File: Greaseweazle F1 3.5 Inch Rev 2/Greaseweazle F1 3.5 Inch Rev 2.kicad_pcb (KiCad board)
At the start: 2 copper layers, 170.2 x 100 mm, 67 parts, among them CN1 Floppy Data, J1 USB B, J10 Conn_01x03, J11 Conn_01x03, J12 Display Port, J13 Display Port, J2 USB Header, J3 Floppy Power, J4 Floppy Power Header, J5 Programming Port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

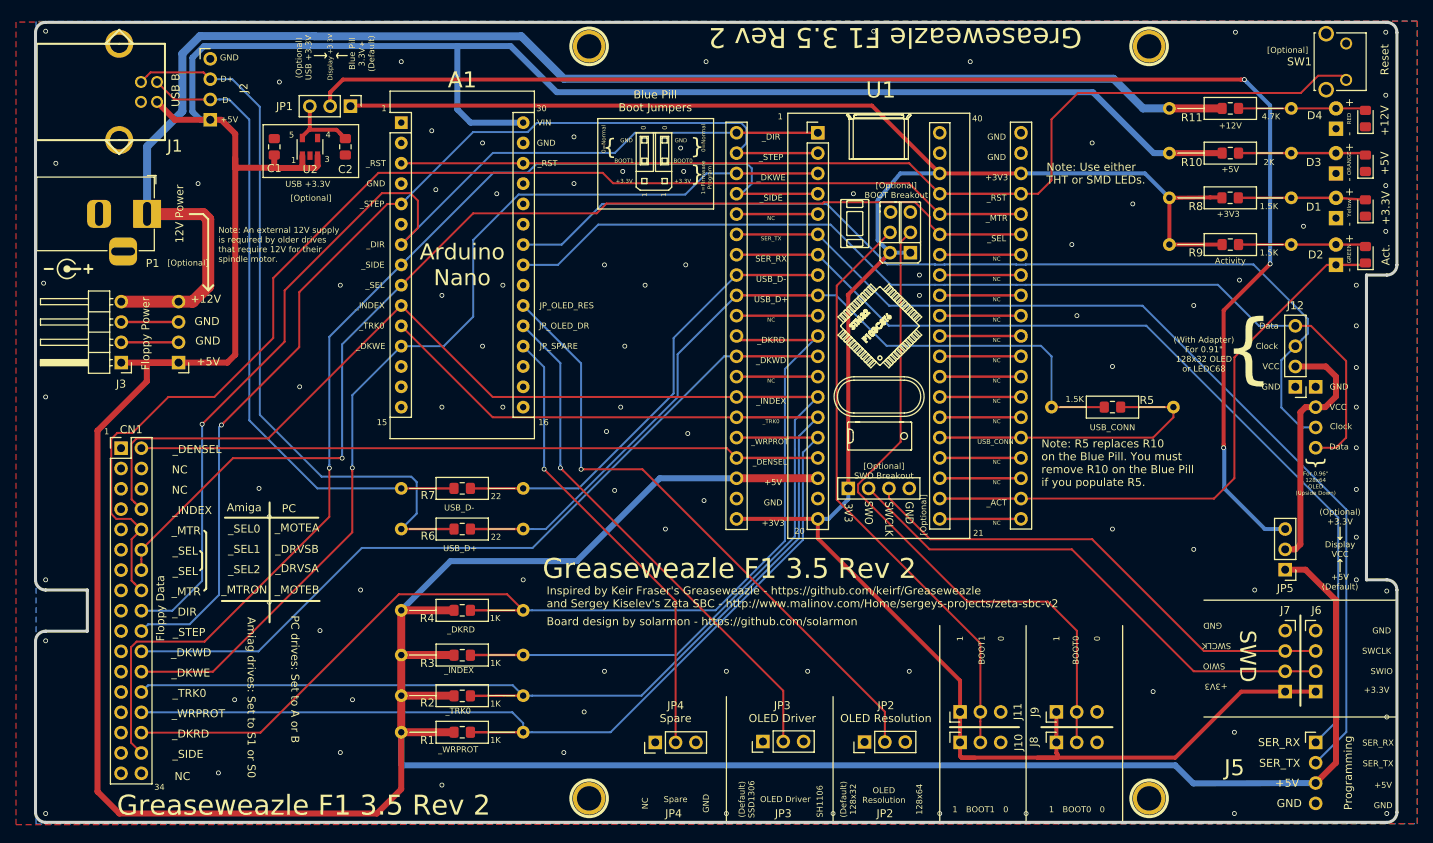
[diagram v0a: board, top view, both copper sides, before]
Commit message: Grounded USB shiled, and improved Arduino Nano silkscreen
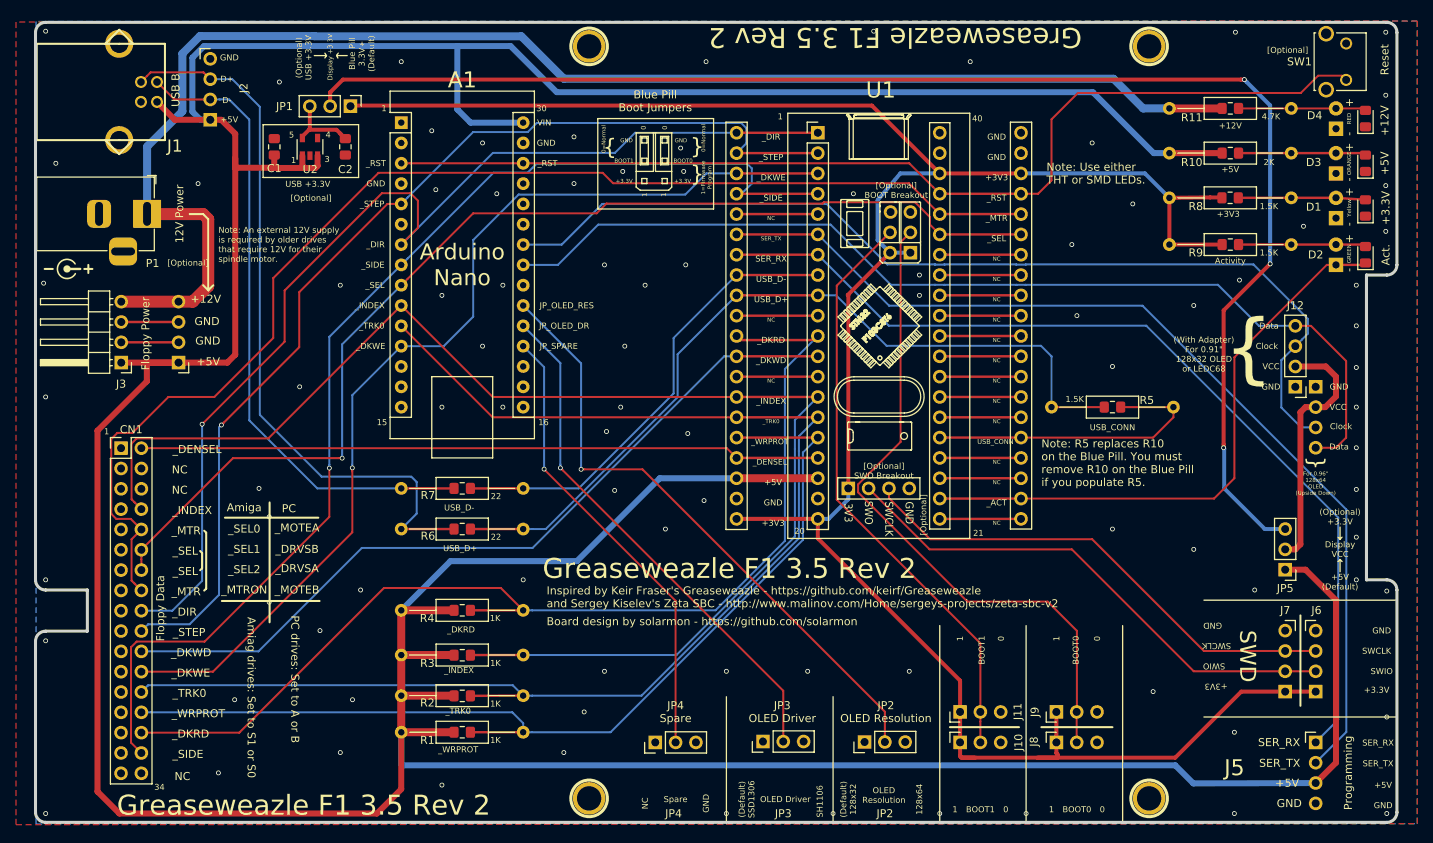
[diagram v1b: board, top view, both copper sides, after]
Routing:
- net /_DKRD: track 137.3 -> 137.9 mm

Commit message: Moved J13 for 0.96 inch OLED further forward
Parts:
- moved Floppy Drive 3.30 mm to (159.0, 100.8)
- moved J13 2.54 mm to (213.4, 96.5)
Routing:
- net /Display_VCC: track 32.3 -> 37.3 mm
- net /Display_Clock: track 123.9 -> 126.5 mm
- net /Display_Data: track 125.9 -> 126.8 mm
- net GND: vias 94 -> 93
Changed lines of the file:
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@@
     (thickness 1.6)
     (drawings 348)
-    (tracks 645)
+    (tracks 643)
     (zones 0)
     (modules 67)
@@
   )
   (module Connector_PinHeader_2.54mm:PinHeader_1x04_P2.54mm_Vertical (layer B.Cu)
-    (at 210.82 96.52 180)
+    (at 213.36 96.52 180)
     (descr "Through hole straight pin header, 1x04, 2.54mm pitch, single row")
     (tags "Through hole pin header THT 1x04 2.54mm single row")
@@
   )
   (module solarmon_library:Floppy_Drive locked (layer F.Cu)
-    (at 155.702 100.838)
+    (at 159 100.838)
     (fp_text reference "Floppy Drive" (at 0.254 -2.032) (layer Dwgs.User)
       (effects (font (size 1 1) (thickness 0.15)))
@@
   (gr_line (start 213.868 118.11) (end 214.122 118.364) (layer F.SilkS) (width 0.12))
   (gr_line (start 213.868 119.634) (end 213.868 118.11) (layer F.SilkS) (width 0.12))
-  (gr_text { (at 210.693 106.045 90) (layer F.SilkS)
+  (gr_text { (at 213.1314 106.3244 90) (layer F.SilkS)
     (effects (font (size 2 2) (thickness 0.125)))
   )
@@
     (effects (font (size 7 7) (thickness 0.125)))
   )
-  (gr_text "For 0.96\"\n128x64\nOLED\n(Upside Down)" (at 210.82 108.585) (layer F.SilkS)
+  (gr_text "For 0.96\"\n128x64\nOLED\n(Upside Down)" (at 213.2584 108.8644) (layer F.SilkS)
     (effects (font (size 0.5 0.5) (thickness 0.125)))
   )
@@
     (effects (font (size 0.75 0.75) (thickness 0.125)))
   )
-  (gr_text Data (at 213.741 104.013) (layer F.SilkS)
+  (gr_text Data (at 215.773 104.0638) (layer F.SilkS)
     (effects (font (size 0.75 0.75) (thickness 0.125)))
   )
-  (gr_text Clock (at 213.995 101.473) (layer F.SilkS)
-    (effects (font (size 0.75 0.75) (thickness 0.125)))
+  (gr_text Clock (at 215.8238 101.6254) (layer F.SilkS)
+    (effects (font (size 0.6 0.6) (thickness 0.125)))
   )
-  (gr_text VCC (at 213.614 99.06) (layer F.SilkS)
-    (effects (font (size 0.75 0.75) (thickness 0.125)))
+  (gr_text VCC (at 215.8492 99.06) (layer F.SilkS)
+    (effects (font (size 0.6 0.6) (thickness 0.125)))
   )
-  (gr_text GND (at 213.741 96.52) (layer F.SilkS)
-    (effects (font (size 0.75 0.75) (thickness 0.125)))
+  (gr_text GND (at 215.773 96.4946) (layer F.SilkS)
+    (effects (font (size 0.6 0.6) (thickness 0.125)))
   )
   (gr_text Data (at 204.978 88.9) (layer F.SilkS)
@@
   (via (at 215.9 83.82) (size 0.6) (drill 0.4) (layers F.Cu B.Cu) (net 1))
   (via (at 215.9 88.9) (size 0.6) (drill 0.4) (layers F.Cu B.Cu) (net 1))
-  (via (at 215.9 94.107) (size 0.6) (drill 0.4) (layers F.Cu B.Cu) (net 1))
-  (via (at 215.9 99.06) (size 0.6) (drill 0.4) (layers F.Cu B.Cu) (net 1))
-  (via (at 215.9 104.14) (size 0.6) (drill 0.4) (layers F.Cu B.Cu) (net 1))
+  (via (at 215.9 91.44) (size 0.6) (drill 0.4) (layers F.Cu B.Cu) (net 1))
+  (via (at 215.9 106.68) (size 0.6) (drill 0.4) (layers F.Cu B.Cu) (net 1))
   (via (at 215.9 109.347) (size 0.6) (drill 0.4) (layers F.Cu B.Cu) (net 1))
   (via (at 215.9 115.316) (size 0.6) (drill 0.4) (layers F.Cu B.Cu) (net 1))
@@
   (segment (start 163.241999 83.775001) (end 164.418001 83.775001) (width 0.25) (layer B.Cu) (net 67))
   (segment (start 163.236198 83.7692) (end 163.241999 83.775001) (width 0.25) (layer B.Cu) (net 67))
-  (segment (start 213.36 104.14) (end 210.82 104.14) (width 0.25) (layer F.Cu) (net 67))
-  (segment (start 214.63 102.87) (end 213.36 104.14) (width 0.25) (layer F.Cu) (net 67))
-  (segment (start 214.63 93.2942) (end 214.63 102.87) (width 0.25) (layer F.Cu) (net 67))
-  (segment (start 208.28 88.9) (end 210.2358 88.9) (width 0.25) (layer F.Cu) (net 67))
-  (segment (start 210.2358 88.9) (end 214.63 93.2942) (width 0.25) (layer F.Cu) (net 67))
+  (segment (start 216.60449 102.49571) (end 214.9602 104.14) (width 0.25) (layer F.Cu) (net 67))
+  (segment (start 214.9602 104.14) (end 213.36 104.14) (width 0.25) (layer F.Cu) (net 67))
+  (segment (start 216.60449 93.79549) (end 216.60449 102.49571) (width 0.25) (layer F.Cu) (net 67))
+  (segment (start 211.709 88.9) (end 216.60449 93.79549) (width 0.25) (layer F.Cu) (net 67))
+  (segment (start 208.28 88.9) (end 211.709 88.9) (width 0.25) (layer F.Cu) (net 67))
   (via (at 118.999 106.8324) (size 0.6) (drill 0.4) (layers F.Cu B.Cu) (net 68))
   (segment (start 111.76 86.36) (end 118.999 93.599) (width 0.25) (layer B.Cu) (net 68))
@@
   (segment (start 174.578001 81.235001) (end 174.583802 81.2292) (width 0.25) (layer B.Cu) (net 75))
   (segment (start 209.8548 88.0364) (end 209.8548 89.8652) (width 0.25) (layer B.Cu) (net 75))
-  (segment (start 209.0166 101.6) (end 210.82 101.6) (width 0.25) (layer B.Cu) (net 75))
+  (segment (start 209.0166 101.6) (end 213.36 101.6) (width 0.25) (layer B.Cu) (net 75))
   (segment (start 206.5274 99.1108) (end 209.0166 101.6) (width 0.25) (layer B.Cu) (net 75))
-  (segment (start 208.28 91.44) (end 206.5274 93.1926) (width 0.25) (layer B.Cu) (net 75))
   (segment (start 206.5274 93.1926) (end 206.5274 99.1108) (width 0.25) (layer B.Cu) (net 75))
+  (segment (start 208.28 91.44) (end 206.5274 93.1926) (width 0.25) (layer B.Cu) (net 75))
   (segment (start 208.0768 93.7768) (end 208.28 93.98) (width 0.25) (layer B.Cu) (net 76))
   (segment (start 208.3054 93.9546) (end 208.28 93.98) (width 0.5) (layer B.Cu) (net 76))
-  (segment (start 212.022082 99.06) (end 210.82 99.06) (width 0.75) (layer F.Cu) (net 76))
-  (segment (start 213.36 97.722082) (end 212.022082 99.06) (width 0.75) (layer F.Cu) (net 76))
-  (segment (start 213.36 95.25) (end 213.36 97.722082) (width 0.75) (layer F.Cu) (net 76))
-  (segment (start 208.28 93.98) (end 212.09 93.98) (width 0.75) (layer F.Cu) (net 76))
-  (segment (start 212.09 93.98) (end 213.36 95.25) (width 0.75) (layer F.Cu) (net 76))
-  (segment (start 209.55 99.06) (end 210.82 99.06) (width 0.75) (layer F.Cu) (net 76))
-  (segment (start 208.915 99.695) (end 209.55 99.06) (width 0.75) (layer F.Cu) (net 76))
-  (segment (start 208.915 116.205) (end 208.915 99.695) (width 0.75) (layer F.Cu) (net 76))
-  (segment (start 207.01 116.84) (end 208.28 116.84) (width 0.75) (layer F.Cu) (net 76))
-  (segment (start 208.28 116.84) (end 208.915 116.205) (width 0.75) (layer F.Cu) (net 76))
+  (segment (start 208.28 116.84) (end 207.01 116.84) (width 0.75) (layer F.Cu) (net 76))
+  (segment (start 208.915 116.205) (end 208.28 116.84) (width 0.75) (layer F.Cu) (net 76))
+  (segment (start 208.915 99.695) (end 208.915 116.205) (width 0.75) (layer F.Cu) (net 76))
+  (segment (start 209.55 99.06) (end 208.915 99.695) (width 0.75) (layer F.Cu) (net 76))
+  (segment (start 215.854479 97.767603) (end 214.562082 99.06) (width 0.75) (layer F.Cu) (net 76))
+  (segment (start 215.854479 95.331479) (end 215.854479 97.767603) (width 0.75) (layer F.Cu) (net 76))
+  (segment (start 214.562082 99.06) (end 209.55 99.06) (width 0.75) (layer F.Cu) (net 76))
+  (segment (start 214.503 93.98) (end 215.854479 95.331479) (width 0.75) (layer F.Cu) (net 76))
+  (segment (start 208.28 93.98) (end 214.503 93.98) (width 0.75) (layer F.Cu) (net 76))
   (zone (net 1) (net_name GND) (layer B.Cu) (hatch edge 0.508)
     (connect_pads (clearance 0.254))
